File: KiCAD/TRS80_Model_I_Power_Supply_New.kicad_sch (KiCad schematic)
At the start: 6 parts, among them J1 Conn_01x02, J2 1x5, T1 DST-6-16

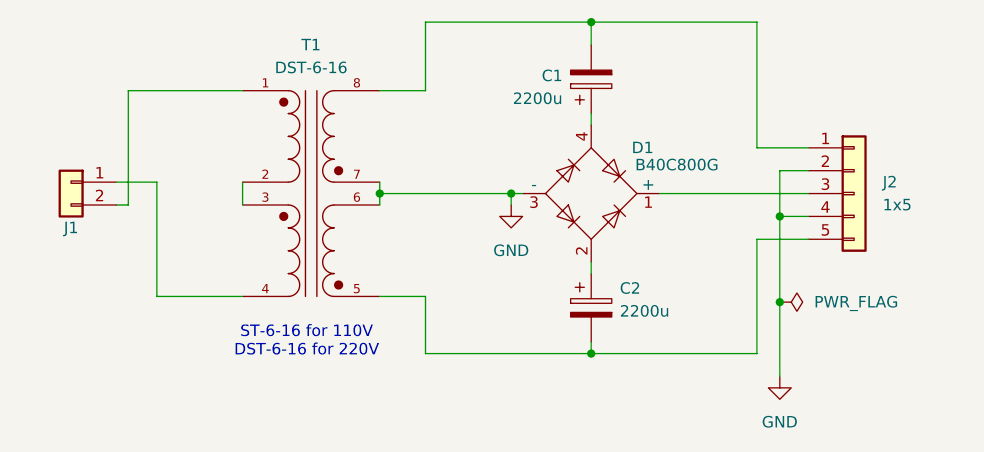
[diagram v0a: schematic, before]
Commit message: Improved documentation
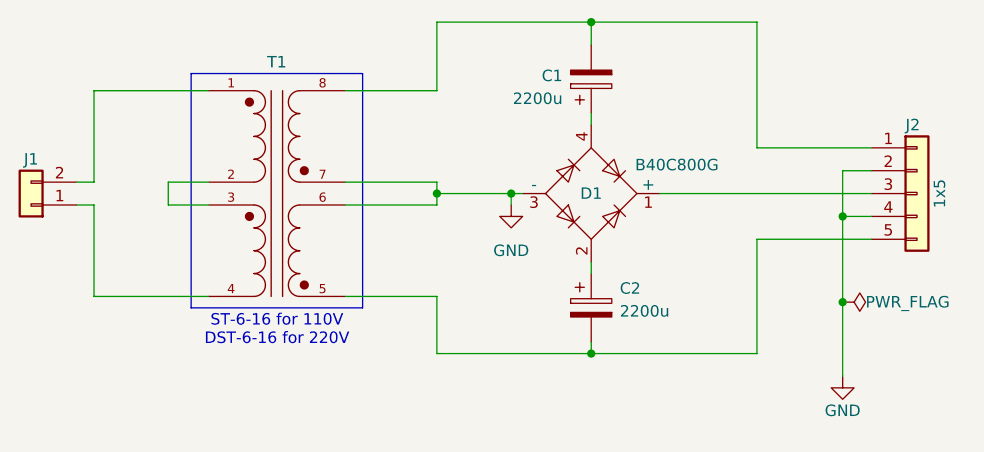
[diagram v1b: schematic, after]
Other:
- moved on the sheet: J1, J2, T1
